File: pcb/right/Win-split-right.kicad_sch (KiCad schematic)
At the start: 175 parts, among them J1 Conn_01x04_Socket, U1 RP2040_ProMicro, U2 74AHCT1G125

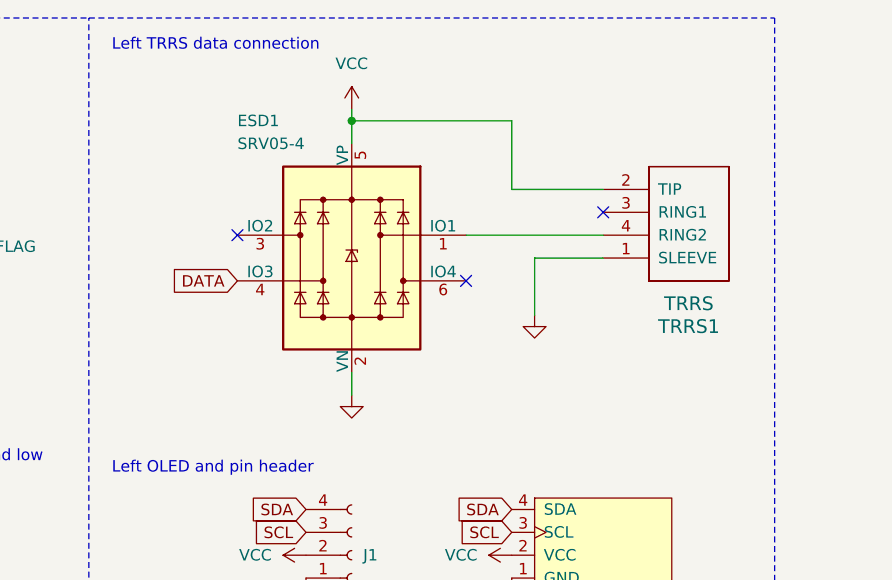
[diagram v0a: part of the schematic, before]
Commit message: vial firmware and 3D cases
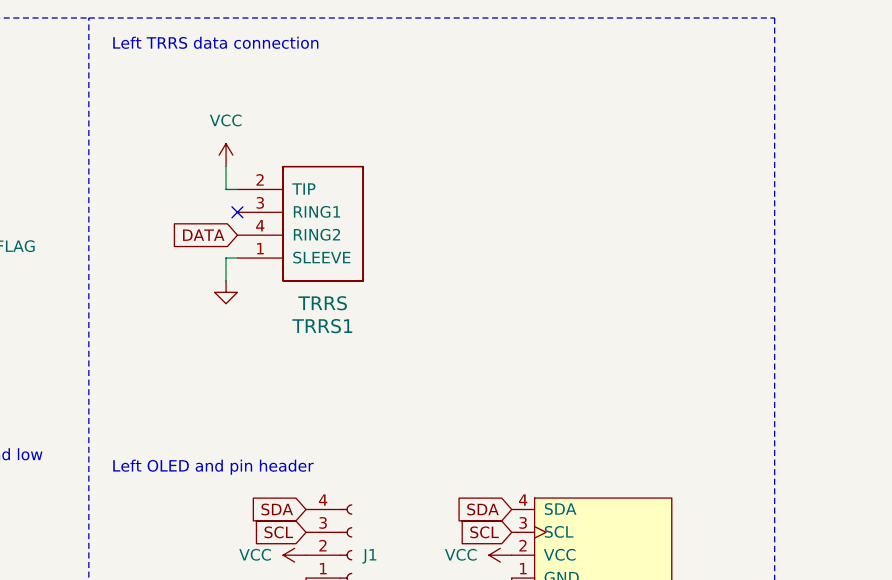
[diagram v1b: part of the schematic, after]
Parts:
- removed ESD1: SRV05-4, PCM_marbastlib-various:SOT-23-6-routable, symbol PCM_marbastlib-various:SRV05-4
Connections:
- net DATA: now also TRRS1.4 (RING2)
- no-connect marks 15 -> 13
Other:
- moved on the sheet: TRRS1
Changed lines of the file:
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@@
   (junction (at 132.08 367.03) (diameter 0) (color 0 0 0 0)
   )
-  (junction (at 116.84 26.67) (diameter 0) (color 0 0 0 0)
-  )
   (junction (at 124.46 256.54) (diameter 0) (color 0 0 0 0)
   )
@@
   (no_connect (at 41.91 67.31))
   (no_connect (at 52.07 67.31))
-  (no_connect (at 144.78 36.83))
-  (no_connect (at 104.14 39.37))
+  (no_connect (at 104.14 36.83))
   (no_connect (at 41.91 30.48))
   (no_connect (at 44.45 67.31))
-  (no_connect (at 129.54 44.45))
   (no_connect (at 39.37 67.31))
   (no_connect (at 59.69 33.02))
   (no_connect (at 317.5 506.73))
-  (wire (pts (xy 134.62 34.29) (xy 144.78 34.29))
-    (stroke (width 0) (type default))
-  )
   (wire (pts (xy 132.08 373.38) (xy 132.08 377.19))
     (stroke (width 0) (type default))
@@
     (stroke (width 0) (type default))
   )
-  (wire (pts (xy 134.62 34.29) (xy 134.62 26.67))
-    (stroke (width 0) (type default))
-  )
   (wire (pts (xy 132.08 424.18) (xy 132.08 430.53))
     (stroke (width 0) (type default))
@@
     (stroke (width 0) (type dash_dot))
   )
-  (wire (pts (xy 116.84 25.4) (xy 116.84 26.67))
-    (stroke (width 0) (type default))
-  )
   (wire (pts (xy 157.48 496.57) (xy 157.48 499.11))
     (stroke (width 0) (type default))
@@
     (stroke (width 0) (type default))
   )
-  (wire (pts (xy 134.62 26.67) (xy 116.84 26.67))
-    (stroke (width 0) (type default))
-  )
   (wire (pts (xy 233.68 496.57) (xy 233.68 499.11))
     (stroke (width 0) (type default))
@@
     (stroke (width 0) (type default))
   )
-  (wire (pts (xy 116.84 26.67) (xy 116.84 29.21))
-    (stroke (width 0) (type default))
-  )
   (wire (pts (xy 309.88 367.03) (xy 325.12 367.03))
     (stroke (width 0) (type default))
@@
     (stroke (width 0) (type default))
   )
-  (wire (pts (xy 116.84 54.61) (xy 116.84 57.15))
-    (stroke (width 0) (type default))
-  )
   (wire (pts (xy 226.06 231.14) (xy 226.06 256.54))
     (stroke (width 0) (type default))
@@
     (stroke (width 0) (type default))
   )
-  (wire (pts (xy 144.78 41.91) (xy 137.16 41.91))
+  (wire (pts (xy 104.14 41.91) (xy 102.87 41.91))
     (stroke (width 0) (type default))
   )
@@
     (stroke (width 0) (type default))
   )
-  (wire (pts (xy 137.16 41.91) (xy 137.16 48.26))
+  (wire (pts (xy 102.87 41.91) (xy 102.87 44.45))
     (stroke (width 0) (type default))
   )
@@
     (stroke (width 0) (type default))
   )
-  (wire (pts (xy 129.54 39.37) (xy 144.78 39.37))
-    (stroke (width 0) (type default))
-  )
   (wire (pts (xy 182.88 400.05) (xy 208.28 400.05))
     (stroke (width 0) (type default))
@@
     (stroke (width 0) (type default))
   )
+  (wire (pts (xy 102.87 34.29) (xy 102.87 31.75))
+    (stroke (width 0) (type default))
+  )
   (wire (pts (xy 233.68 373.38) (xy 233.68 377.19))
     (stroke (width 0) (type default))
@@
     (stroke (width 0) (type default))
   )
+  (wire (pts (xy 104.14 34.29) (xy 102.87 34.29))
+    (stroke (width 0) (type default))
+  )
   (wire (pts (xy 132.08 392.43) (xy 132.08 400.05))
     (stroke (width 0) (type default))
@@
     )
   )
-  (global_label "DATA" (shape input) (at 104.14 44.45 180) (fields_autoplaced)
-    (effects (font (size 1.27 1.27)) (justify right))
-    (property "Intersheetrefs" "${INTERSHEET_REFS}" (at 96.74 44.45 0)
-      (effects (font (size 1.27 1.27)) (justify right) hide)
-    )
-  )
   (global_label "RESET" (shape input) (at 34.29 40.64 180) (fields_autoplaced)
     (effects (font (size 1.27 1.27)) (justify right))
@@
     )
   )
+  (global_label "DATA" (shape input) (at 104.14 39.37 180) (fields_autoplaced)
+    (effects (font (size 1.27 1.27)) (justify right))
+    (property "Intersheetrefs" "${INTERSHEET_REFS}" (at 96.74 39.37 0)
+      (effects (font (size 1.27 1.27)) (justify right) hide)
+    )
+  )
   (global_label "LED_5v" (shape input) (at 312.42 341.63 0) (fields_autoplaced)
     (effects (font (size 1.27 1.27)) (justify left))
@@
     )
   )
-  (symbol (lib_id "ScottoKeebs:Placeholder_TRRS") (at 153.67 44.45 0) (unit 1)
+  (symbol (lib_id "ScottoKeebs:Placeholder_TRRS") (at 113.03 44.45 0) (unit 1)
     (in_bom yes) (on_board yes) (dnp no)
-    (property "Reference" "TRRS1" (at 154.305 49.53 0)
+    (property "Reference" "TRRS1" (at 113.665 49.53 0)
       (effects (font (size 1.524 1.524)))
     )
-    (property "Value" "TRRS" (at 154.305 46.99 0)
+    (property "Value" "TRRS" (at 113.665 46.99 0)
       (effects (font (size 1.524 1.524)))
     )
-    (property "Footprint" "ScottoKeebs_Components:TRRS_PJ-320A" (at 157.48 44.45 0)
+    (property "Footprint" "ScottoKeebs_Components:TRRS_PJ-320A" (at 116.84 44.45 0)
       (effects (font (size 1.524 1.524)) hide)
     )
-    (property "Datasheet" "" (at 157.48 44.45 0)
+    (property "Datasheet" "" (at 116.84 44.45 0)
       (effects (font (size 1.524 1.524)) hide)
     )
@@
     )
   )
-  (symbol (lib_id "power:GND") (at 116.84 57.15 0) (mirror y) (unit 1)
-    (in_bom yes) (on_board yes) (dnp no)
-    (property "Reference" "#PWR022" (at 116.84 63.5 0)
-      (effects (font (size 1.27 1.27)) hide)
-    )
-    (property "Value" "GND" (at 116.713 61.5442 0)
-      (effects (font (size 1.27 1.27)) hide)
-    )
-    (property "Footprint" "" (at 116.84 57.15 0)
-      (effects (font (size 1.27 1.27)) hide)
-    )
-    (property "Datasheet" "" (at 116.84 57.15 0)
-      (effects (font (size 1.27 1.27)) hide)
-    )
-    (pin "1")
-    (instances
-      (project "Win-split-right"
-        (path "/49098896-502f-4162-bad5-517f7d921ed4"
-          (reference "#PWR022") (unit 1)
-        )
-      )
-    )
-  )
   (symbol (lib_id "Device:C_Small") (at 261.62 485.14 90) (unit 1)
     (in_bom yes) (on_board yes) (dnp no)
@@
     )
   )
-  (symbol (lib_name "GND_2") (lib_id "power:GND") (at 137.16 48.26 0) (mirror y) (unit 1)
+  (symbol (lib_name "GND_2") (lib_id "power:GND") (at 102.87 44.45 0) (mirror y) (unit 1)
     (in_bom yes) (on_board yes) (dnp no) (fields_autoplaced)
-    (property "Reference" "#PWR09" (at 137.16 54.61 0)
+    (property "Reference" "#PWR09" (at 102.87 50.8 0)
       (effects (font (size 1.27 1.27)) hide)
     )
-    (property "Value" "GND" (at 137.16 52.07 90)
+    (property "Value" "GND" (at 102.87 48.26 90)
       (effects (font (size 1.27 1.27)) (justify right) hide)
     )
-    (property "Footprint" "" (at 137.16 48.26 0)
+    (property "Footprint" "" (at 102.87 44.45 0)
       (effects (font (size 1.27 1.27)) hide)
     )
-    (property "Datasheet" "" (at 137.16 48.26 0)
+    (property "Datasheet" "" (at 102.87 44.45 0)
       (effects (font (size 1.27 1.27)) hide)
     )
@@
     )
   )
-  (symbol (lib_id "PCM_marbastlib-various:SRV05-4") (at 116.84 41.91 0) (mirror y) (unit 1)
-    (in_bom yes) (on_board yes) (dnp no)
-    (property "Reference" "ESD1" (at 104.14 26.67 0)
-      (effects (font (size 1.27 1.27)) (justify right))
-    )
-    (property "Value" "SRV05-4" (at 104.14 29.21 0)
-      (effects (font (size 1.27 1.27)) (justify right))
-    )
-    (property "Footprint" "PCM_marbastlib-various:SOT-23-6-routable" (at 99.06 53.34 0)
-      (effects (font (size 1.27 1.27)) hide)
-    )
-    (property "Datasheet" "http://www.onsemi.com/pub/Collateral/SRV05-4-D.PDF" (at 116.84 41.91 0)
-      (effects (font (size 1.27 1.27)) hide)
-    )
-    (property "LCSC" "C558418" (at 116.84 41.91 0)
-      (effects (font (size 1.27 1.27)) hide)
-    )
-    (pin "1")
-    (pin "2")
-    (pin "3")
-    (pin "4")
-    (pin "5")
-    (pin "6")
-    (instances
-      (project "Win-split-right"
-        (path "/49098896-502f-4162-bad5-517f7d921ed4"
-          (reference "ESD1") (unit 1)
-        )
-      )
-    )
-  )
   (symbol (lib_id "ScottoKeebs:Placeholder_Diode") (at 154.94 214.63 90) (unit 1)
     (in_bom yes) (on_board yes) (dnp no) (fields_autoplaced)
@@
     )
   )
-  (symbol (lib_id "power:VCC") (at 116.84 25.4 0) (mirror y) (unit 1)
+  (symbol (lib_id "power:VCC") (at 102.87 31.75 0) (mirror y) (unit 1)
     (in_bom yes) (on_board yes) (dnp no) (fields_autoplaced)
-    (property "Reference" "#PWR03" (at 116.84 29.21 0)
+    (property "Reference" "#PWR03" (at 102.87 35.56 0)
       (effects (font (size 1.27 1.27)) hide)
     )
-    (property "Value" "VCC" (at 116.84 20.32 0)
+    (property "Value" "VCC" (at 102.87 26.67 0)
       (effects (font (size 1.27 1.27)))
     )
-    (property "Footprint" "" (at 116.84 25.4 0)
+    (property "Footprint" "" (at 102.87 31.75 0)
       (effects (font (size 1.27 1.27)) hide)
     )
-    (property "Datasheet" "" (at 116.84 25.4 0)
+    (property "Datasheet" "" (at 102.87 31.75 0)
       (effects (font (size 1.27 1.27)) hide)
     )
